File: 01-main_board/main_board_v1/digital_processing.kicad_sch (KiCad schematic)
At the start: 26 parts, among them IC9 LSF0108PWR, T1 749013011

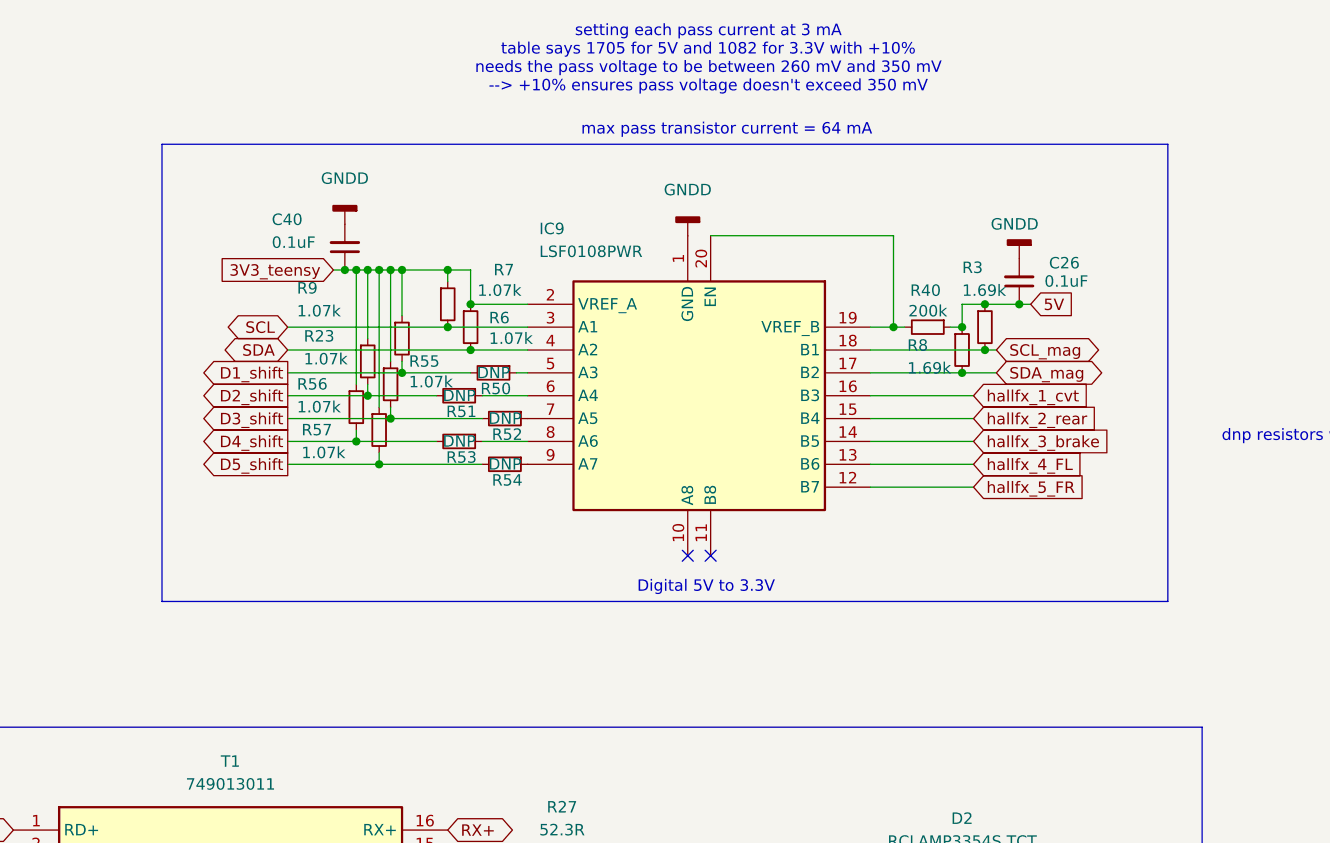
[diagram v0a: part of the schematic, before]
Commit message: added spark plug digital input
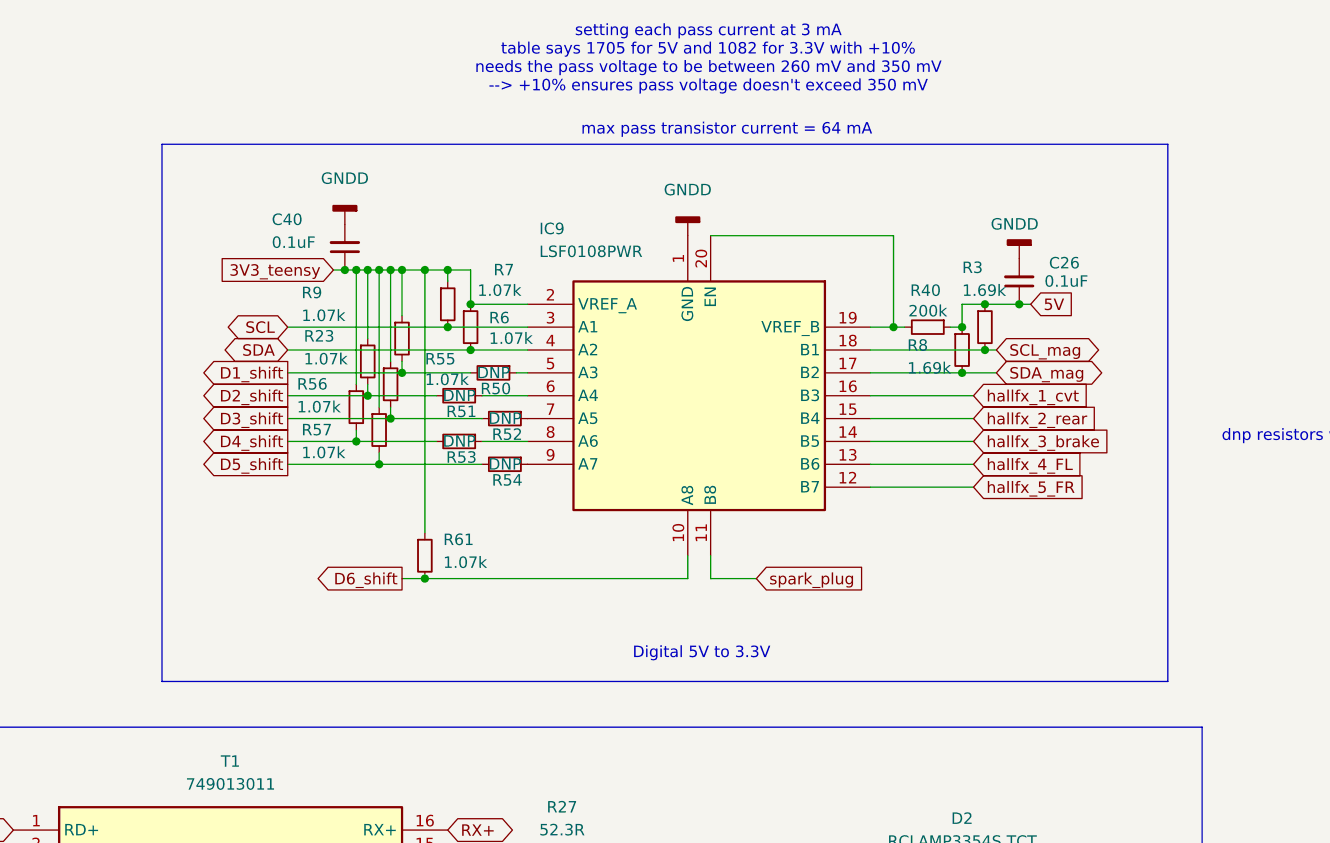
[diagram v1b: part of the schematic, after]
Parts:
- added R61: 1.07k, Resistor_SMD:R_0402_1005Metric, symbol Device:R_Small
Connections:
- net 3V3_teensy: now also R61.1
- net D6_shift: now reaches IC9.10 (A8)
- net D6_shift: now also R61.2
- net spark_plug: now reaches IC9.11 (B8)
- no-connect marks 6 -> 4
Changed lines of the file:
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@@
 	(rectangle
 		(start 118.11 52.07)
-		(end 229.87 102.87)
+		(end 229.87 111.76)
 		(stroke
 			(width 0)
@@
 	(text "Digital 5V to 3.3V"
 		(exclude_from_sim no)
-		(at 178.562 101.346 0)
+		(at 178.054 108.712 0)
 		(effects
 			(font
@@
 	)
 	(junction
+		(at 147.32 100.33)
+		(diameter 0)
+		(color 0 0 0 0)
+	)
+	(junction
 		(at 85.09 143.51)
 		(diameter 0)
@@
 	)
 	(junction
+		(at 147.32 66.04)
+		(diameter 0)
+		(color 0 0 0 0)
+	)
+	(junction
 		(at 85.09 130.81)
 		(diameter 0)
@@
 	)
 	(no_connect
-		(at 179.07 97.79)
-	)
-	(no_connect
 		(at 101.6 138.43)
 	)
@@
 	)
 	(no_connect
-		(at 176.53 97.79)
-	)
-	(no_connect
 		(at 101.6 135.89)
 	)
 	(wire
 		(pts
+			(xy 147.32 100.33) (xy 176.53 100.33)
+		)
+		(stroke
+			(width 0)
+			(type default)
+		)
+	)
+	(wire
+		(pts
 			(xy 166.37 143.51) (xy 165.1 143.51)
 		)
@@
 	(wire
 		(pts
+			(xy 179.07 100.33) (xy 179.07 97.79)
+		)
+		(stroke
+			(width 0)
+			(type default)
+		)
+	)
+	(wire
+		(pts
 			(xy 77.47 143.51) (xy 85.09 143.51)
 		)
@@
 	(wire
 		(pts
-			(xy 144.78 66.04) (xy 149.86 66.04)
+			(xy 144.78 66.04) (xy 147.32 66.04)
 		)
 		(stroke
@@
 	(wire
 		(pts
+			(xy 144.78 100.33) (xy 147.32 100.33)
+		)
+		(stroke
+			(width 0)
+			(type default)
+		)
+	)
+	(wire
+		(pts
 			(xy 77.47 130.81) (xy 85.09 130.81)
 		)
@@
 	(wire
 		(pts
+			(xy 184.15 100.33) (xy 179.07 100.33)
+		)
+		(stroke
+			(width 0)
+			(type default)
+		)
+	)
+	(wire
+		(pts
 			(xy 139.7 83.82) (xy 139.7 85.09)
 		)
@@
 	(wire
 		(pts
+			(xy 147.32 66.04) (xy 147.32 95.25)
+		)
+		(stroke
+			(width 0)
+			(type default)
+		)
+	)
+	(wire
+		(pts
 			(xy 142.24 87.63) (xy 153.67 87.63)
 		)
@@
 	(wire
 		(pts
+			(xy 147.32 66.04) (xy 149.86 66.04)
+		)
+		(stroke
+			(width 0)
+			(type default)
+		)
+	)
+	(wire
+		(pts
 			(xy 196.85 87.63) (xy 208.28 87.63)
 		)
@@
 		(pts
 			(xy 140.97 66.04) (xy 142.24 66.04)
+		)
+		(stroke
+			(width 0)
+			(type default)
+		)
+	)
+	(wire
+		(pts
+			(xy 176.53 97.79) (xy 176.53 100.33)
 		)
 		(stroke
@@
 		)
 	)
+	(global_label "D6_shift"
+		(shape output)
+		(at 144.78 100.33 180)
+		(fields_autoplaced yes)
+		(effects
+			(font
+				(size 1.27 1.27)
+			)
+			(justify right)
+		)
+		(property "Intersheetrefs" "${INTERSHEET_REFS}"
+			(at 134.1144 100.33 0)
+			(effects
+				(font
+					(size 1.27 1.27)
+				)
+				(justify right)
+				(hide yes)
+			)
+		)
+	)
 	(global_label "5V"
 		(shape input)
@@
 		(property "Intersheetrefs" "${INTERSHEET_REFS}"
 			(at 171.8599 68.0262 0)
+			(effects
+				(font
+					(size 1.27 1.27)
+				)
+				(justify left)
+				(hide yes)
+			)
+		)
+	)
+	(global_label "spark_plug"
+		(shape input)
+		(at 184.15 100.33 0)
+		(fields_autoplaced yes)
+		(effects
+			(font
+				(face "KiCad Font")
+				(size 1.27 1.27)
+			)
+			(justify left)
+		)
+		(property "Intersheetrefs" "${INTERSHEET_REFS}"
+			(at 197.3554 100.33 0)
 			(effects
 				(font
@@
 		(dnp no)
 		(property "Reference" "R55"
-			(at 145.542 76.2 0)
+			(at 147.32 75.946 0)
 			(effects
 				(font
@@
 		)
 		(property "Value" "1.07k"
-			(at 145.542 78.486 0)
+			(at 147.32 78.232 0)
 			(effects
 				(font
@@
 		(dnp no)
 		(property "Reference" "R9"
-			(at 133.096 68.072 0)
+			(at 133.604 68.58 0)
 			(effects
 				(font
@@
 		)
 		(property "Value" "1.07k"
-			(at 133.096 70.612 0)
+			(at 133.604 71.12 0)
 			(effects
 				(font
@@
 					(unit 1)
 				)
+			)
+		)
+	)
+	(symbol
+		(lib_id "Device:R_Small")
+		(at 147.32 97.79 0)
+		(unit 1)
+		(exclude_from_sim no)
+		(in_bom yes)
+		(on_board yes)
+		(dnp no)
+		(property "Reference" "R61"
+			(at 149.352 96.012 0)
+			(effects
+				(font
+					(size 1.27 1.27)
+				)
+				(justify left)
+			)
+		)
+		(property "Value" "1.07k"
+			(at 149.352 98.552 0)
+			(effects
+				(font
+					(size 1.27 1.27)
+				)
+				(justify left)
+			)
+		)
+		(property "Footprint" "Resistor_SMD:R_0402_1005Metric"
+			(at 147.32 97.79 0)
+			(effects
+				(font
+					(size 1.27 1.27)
+				)
+				(hide yes)
+			)
+		)
+		(property "Datasheet" "~"
+			(at 147.32 97.79 0)
+			(effects
+				(font
+					(size 1.27 1.27)
+				)
+				(hide yes)
+			)
+		)
+		(property "Description" "Resistor, small symbol"
+			(at 147.32 97.79 0)
+			(effects
+				(font
+					(size 1.27 1.27)
+				)
+				(hide yes)
+			)
+		)
+		(pin "1"
+		)
+		(pin "2"
+		)
+		(instances
+			(project "main_board_v1"
+				(path "/12c2237c-5932-49af-9119-92b28c846ae7/1c0fa17f-7333-433d-8099-fbcba82c3572"
+					(reference "R61")
+					(unit 1)
+				)

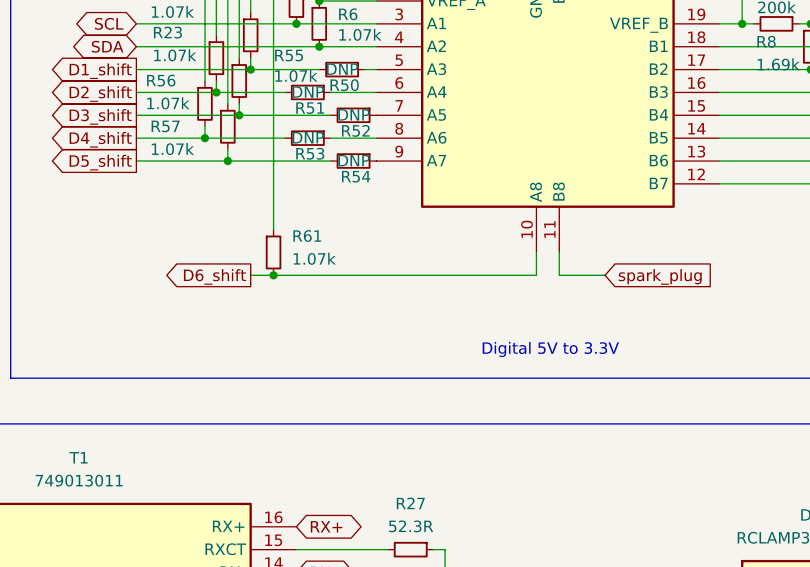
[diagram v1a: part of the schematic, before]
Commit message: grouped externals/ics on layout
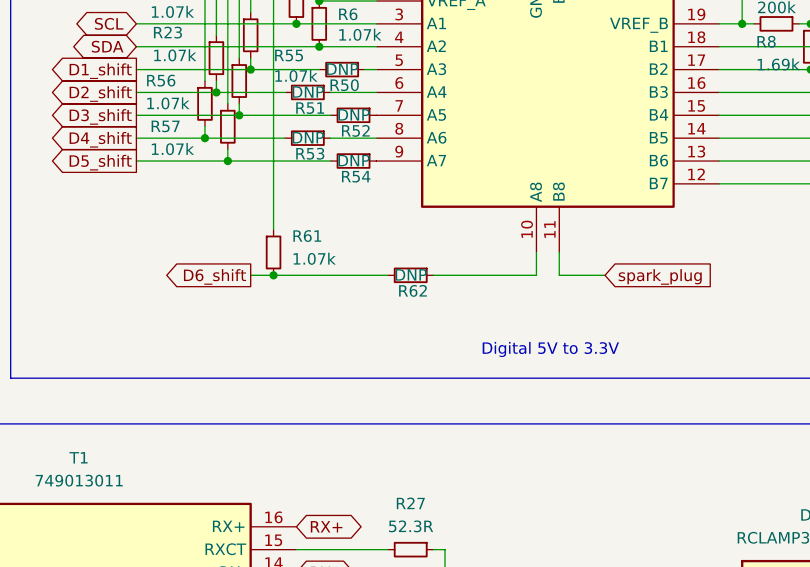
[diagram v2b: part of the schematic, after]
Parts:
- added R62: DNP, Resistor_SMD:R_0402_1005Metric, symbol Device:R_Small
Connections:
- net D6_shift: now also R62.2; no longer IC9.10 (A8)
- new net: IC9.10 (A8), R62.1
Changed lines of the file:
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@@
 	(wire
 		(pts
-			(xy 147.32 100.33) (xy 176.53 100.33)
+			(xy 147.32 100.33) (xy 160.02 100.33)
 		)
 		(stroke
@@
 	(wire
 		(pts
+			(xy 165.1 100.33) (xy 176.53 100.33)
+		)
+		(stroke
+			(width 0)
+			(type default)
+		)
+	)
+	(wire
+		(pts
 			(xy 138.43 66.04) (xy 139.7 66.04)
 		)
@@
 					(unit 1)
 				)
+			)
+		)
+	)
+	(symbol
+		(lib_id "Device:R_Small")
+		(at 162.56 100.33 270)
+		(unit 1)
+		(exclude_from_sim no)
+		(in_bom yes)
+		(on_board yes)
+		(dnp no)
+		(property "Reference" "R62"
+			(at 162.814 102.108 90)
+			(effects
+				(font
+					(size 1.27 1.27)
+				)
+			)
+		)
+		(property "Value" "DNP"
+			(at 162.56 100.33 90)
+			(effects
+				(font
+					(size 1.27 1.27)
+				)
+			)
+		)
+		(property "Footprint" "Resistor_SMD:R_0402_1005Metric"
+			(at 162.56 100.33 0)
+			(effects
+				(font
+					(size 1.27 1.27)
+				)
+				(hide yes)
+			)
+		)
+		(property "Datasheet" "~"
+			(at 162.56 100.33 0)
+			(effects
+				(font
+					(size 1.27 1.27)
+				)
+				(hide yes)
+			)
+		)
+		(property "Description" "Resistor, small symbol"
+			(at 162.56 100.33 0)
+			(effects
+				(font
+					(size 1.27 1.27)
+				)
+				(hide yes)
+			)
+		)
+		(pin "1"
+		)
+		(pin "2"
+		)
+		(instances
+			(project "main_board_v1"
+				(path "/12c2237c-5932-49af-9119-92b28c846ae7/1c0fa17f-7333-433d-8099-fbcba82c3572"
+					(reference "R62")
+					(unit 1)
+				)

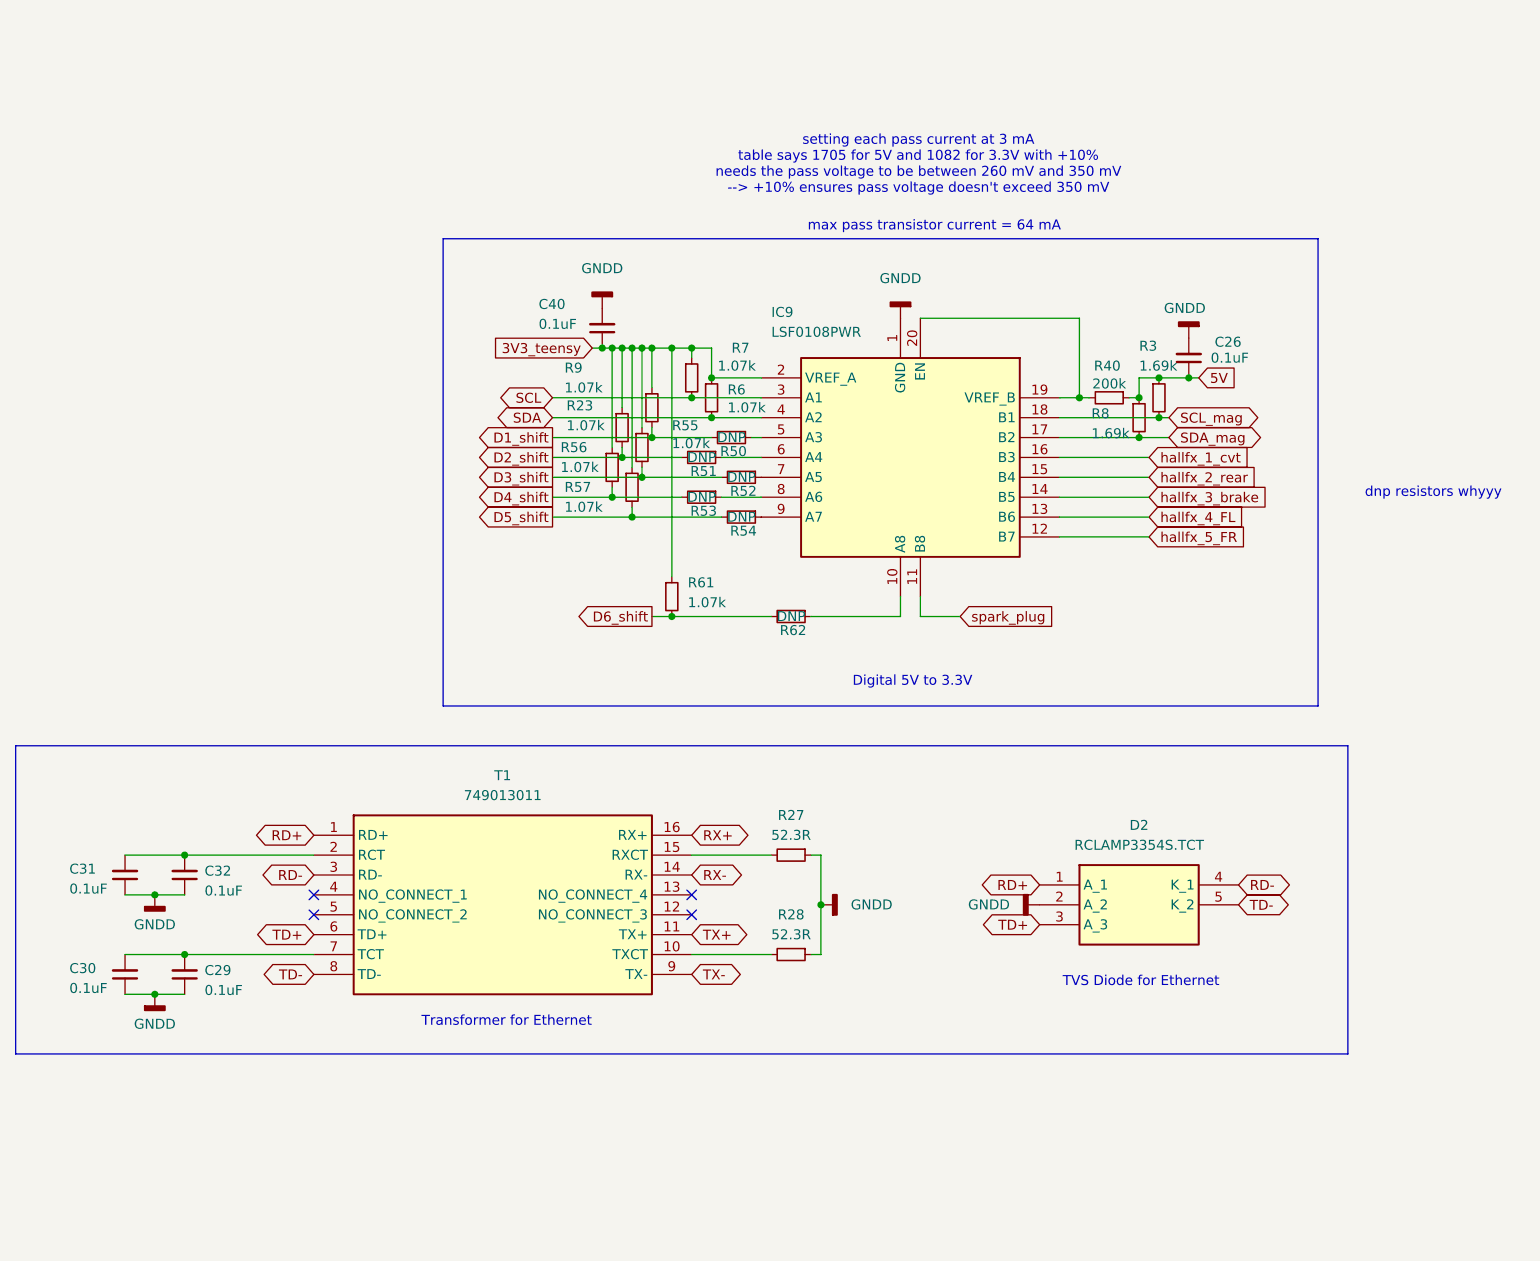
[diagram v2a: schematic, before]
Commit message: added alternate level shifter pathways
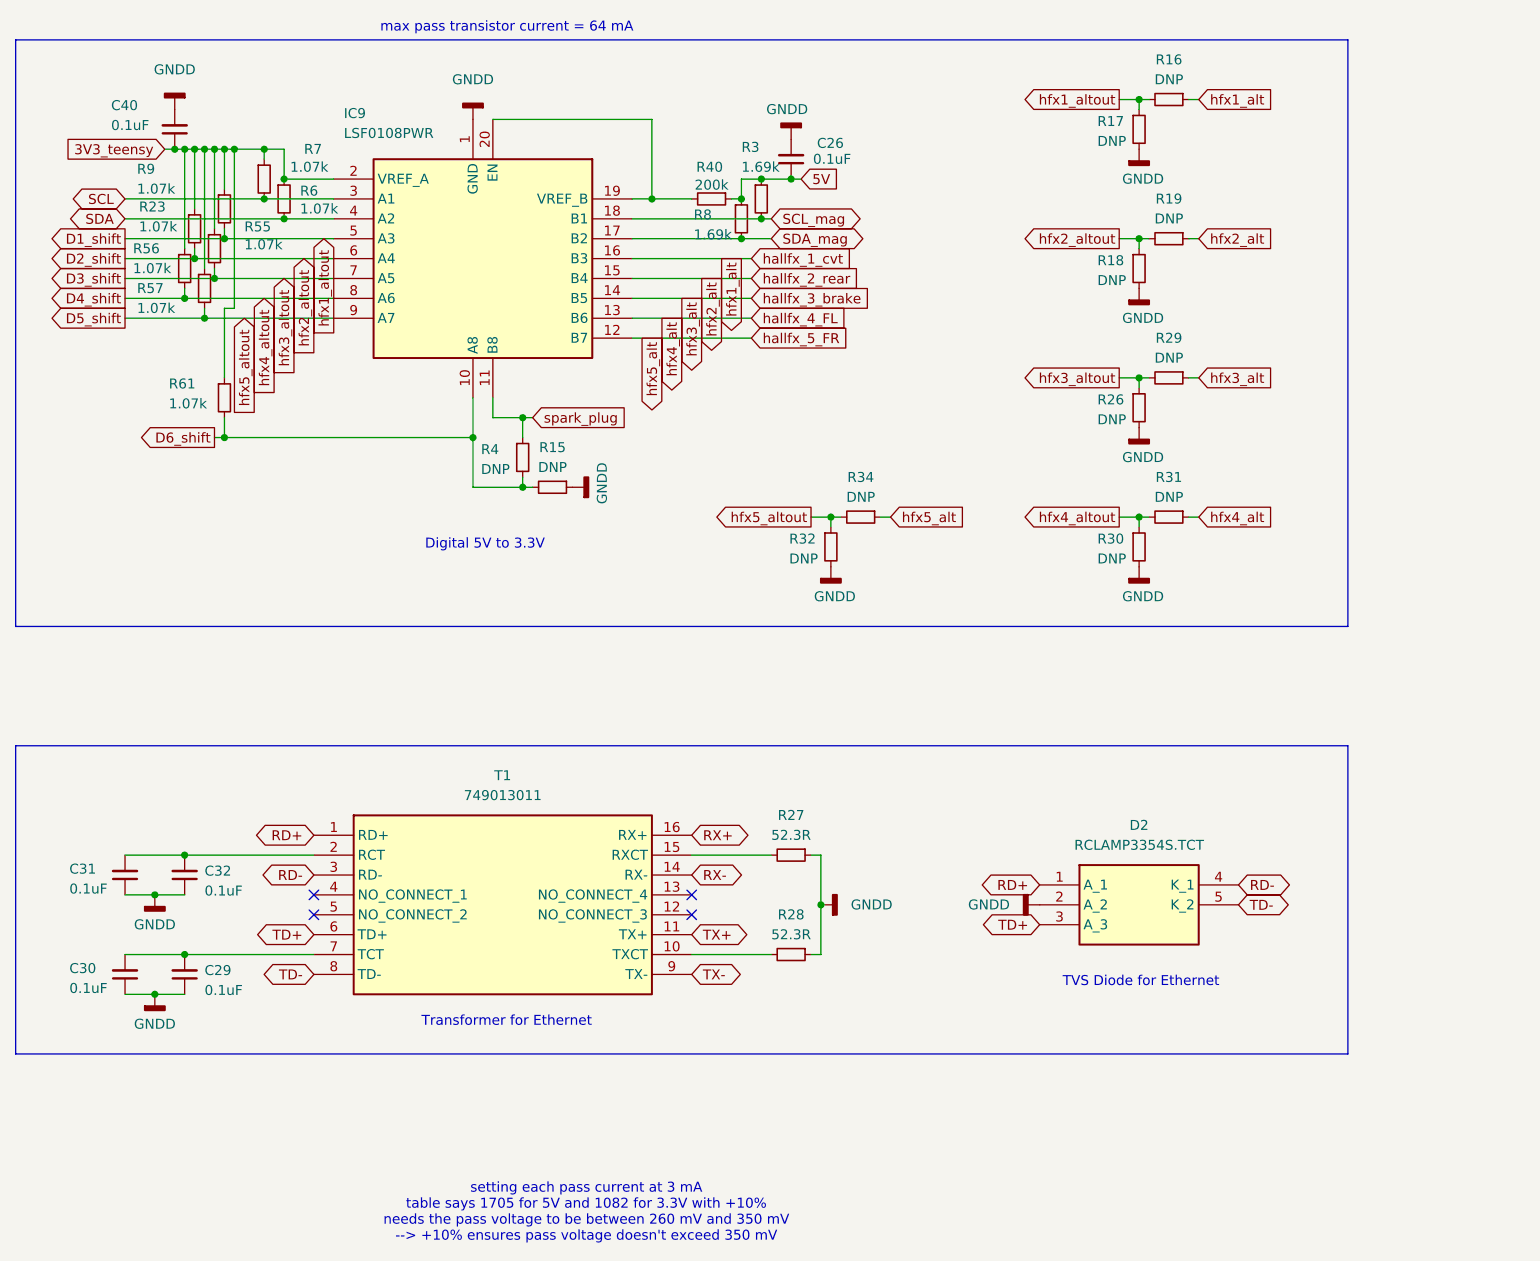
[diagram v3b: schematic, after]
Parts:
- removed R50, R51, R52, R53, R54, R62: DNP, Resistor_SMD:R_0402_1005Metric, symbol Device:R_Small
- added R15, R16, R17, R18, R19, R26, R29, R30, R31, R32, R34, R4: DNP, symbol Device:R_Small
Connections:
- net D1_shift: now also IC9.5 (A3), R16.2, R17.1
- net D2_shift: now also IC9.6 (A4), R18.1, R19.2
- net D3_shift: now also IC9.7 (A5), R26.1, R29.2
- net D4_shift: now also IC9.8 (A6), R30.1, R31.2
- net D5_shift: now also IC9.9 (A7), R32.1, R34.2
- net D6_shift: now also IC9.10 (A8), R15.2, R4.2
- net GNDD: now also R15.1, R17.2, R18.2, R26.2, R30.2, R32.2
- net hallfx_1_cvt: now also R16.1
- net hallfx_2_rear: now also R19.1
- net hallfx_3_brake: now also R29.1
- net hallfx_4_FL: now also R31.1
- net hallfx_5_FR: now also R34.1
- net spark_plug: now also R4.1
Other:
- note removed: "dnp resistors whyyy"
- moved on the sheet: C26, C40, IC9, R23, R3, R40, R55, R56, R57, R6, R61, R7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
